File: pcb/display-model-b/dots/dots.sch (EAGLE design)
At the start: 4 parts

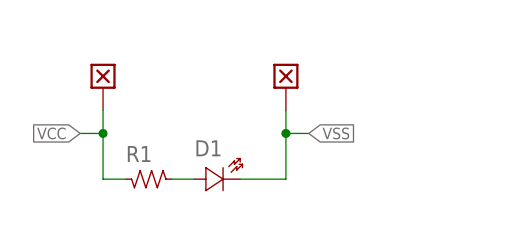
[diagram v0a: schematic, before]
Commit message: Added Model B drawings
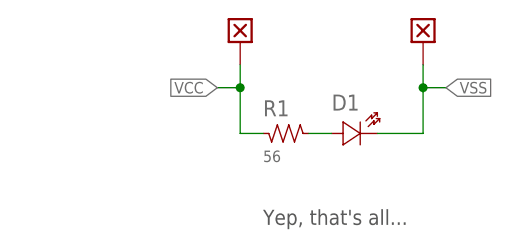
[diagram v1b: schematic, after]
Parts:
- R1: value (none) -> 56
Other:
- note added: "Yep, that's all..."
- moved on the sheet: D1, R1
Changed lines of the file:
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@@
 <schematic xreflabel="%F%N/%S.%C%R" xrefpart="/%S.%C%R">
 <attributes>
+<attribute name="APVD" value=" "/>
+<attribute name="DOC_ID" value="CLK-SCH-06"/>
+<attribute name="DOC_PART_NO" value="CLK-PC-06"/>
+<attribute name="DOC_REV" value="A"/>
+<attribute name="DOC_SUBTITLE" value=" "/>
+<attribute name="DOC_TITLE" value="Dots"/>
+<attribute name="PROJECT_NAME" value="Alarm Clock (Model B)"/>
 </attributes>
 <variantdefs>
@@
 <part name="W1" library="Misc" deviceset="WIRE" device=""/>
 <part name="W2" library="Misc" deviceset="WIRE" device=""/>
-<part name="R1" library="Passive" deviceset="RES" device="-0603"/>
+<part name="R1" library="Passive" deviceset="RES" device="-0603" value="56"/>
 </parts>
 <sheets>
 <sheet>
 <plain>
+<text x="187.96" y="127" size="1.6764" layer="97">Yep, that's all...</text>
 </plain>
 <instances>
 <instance part="FRAME1" gate="G$1" x="0" y="0"/>
-<instance part="D1" gate="G$1" x="182.88" y="132.08"/>
-<instance part="W1" gate="G$1" x="170.18" y="142.24" rot="R90"/>
-<instance part="W2" gate="G$1" x="190.5" y="142.24" rot="R90"/>
-<instance part="R1" gate="A" x="175.26" y="132.08"/>
+<instance part="D1" gate="G$1" x="198.12" y="137.16"/>
+<instance part="W1" gate="G$1" x="185.42" y="147.32" rot="R90"/>
+<instance part="W2" gate="G$1" x="205.74" y="147.32" rot="R90"/>
+<instance part="R1" gate="A" x="190.5" y="137.16"/>
 </instances>
 <busses>
@@
 <segment>
 <pinref part="W1" gate="G$1" pin="P$1"/>
-<wire x1="170.18" y1="139.7" x2="170.18" y2="137.16" width="0.1524" layer="91"/>
+<wire x1="185.42" y1="144.78" x2="185.42" y2="142.24" width="0.1524" layer="91"/>
 <pinref part="R1" gate="A" pin="1"/>
-<wire x1="170.18" y1="137.16" x2="170.18" y2="132.08" width="0.1524" layer="91"/>
-<wire x1="172.72" y1="132.08" x2="170.18" y2="132.08" width="0.1524" layer="91"/>
-<label x="167.64" y="137.16" size="1.27" layer="95" rot="R180" xref="yes"/>
-<wire x1="167.64" y1="137.16" x2="170.18" y2="137.16" width="0.1524" layer="91"/>
-<junction x="170.18" y="137.16"/>
+<wire x1="185.42" y1="142.24" x2="185.42" y2="137.16" width="0.1524" layer="91"/>
+<wire x1="187.96" y1="137.16" x2="185.42" y2="137.16" width="0.1524" layer="91"/>
+<label x="182.88" y="142.24" size="1.27" layer="95" rot="R180" xref="yes"/>
+<wire x1="182.88" y1="142.24" x2="185.42" y2="142.24" width="0.1524" layer="91"/>
+<junction x="185.42" y="142.24"/>
 </segment>
 </net>
@@
 <pinref part="R1" gate="A" pin="2"/>
 <pinref part="D1" gate="G$1" pin="A"/>
-<wire x1="177.8" y1="132.08" x2="180.34" y2="132.08" width="0.1524" layer="91"/>
+<wire x1="193.04" y1="137.16" x2="195.58" y2="137.16" width="0.1524" layer="91"/>
 </segment>
 </net>
@@
 <segment>
 <pinref part="D1" gate="G$1" pin="K"/>
-<wire x1="185.42" y1="132.08" x2="190.5" y2="132.08" width="0.1524" layer="91"/>
+<wire x1="200.66" y1="137.16" x2="205.74" y2="137.16" width="0.1524" layer="91"/>
 <pinref part="W2" gate="G$1" pin="P$1"/>
-<wire x1="190.5" y1="132.08" x2="190.5" y2="137.16" width="0.1524" layer="91"/>
-<label x="193.04" y="137.16" size="1.27" layer="95" xref="yes"/>
-<wire x1="190.5" y1="137.16" x2="190.5" y2="139.7" width="0.1524" layer="91"/>
-<wire x1="190.5" y1="137.16" x2="193.04" y2="137.16" width="0.1524" layer="91"/>
-<junction x="190.5" y="137.16"/>
+<wire x1="205.74" y1="137.16" x2="205.74" y2="142.24" width="0.1524" layer="91"/>
+<label x="208.28" y="142.24" size="1.27" layer="95" xref="yes"/>
+<wire x1="205.74" y1="142.24" x2="205.74" y2="144.78" width="0.1524" layer="91"/>
+<wire x1="205.74" y1="142.24" x2="208.28" y2="142.24" width="0.1524" layer="91"/>
+<junction x="205.74" y="142.24"/>
 </segment>
 </net>

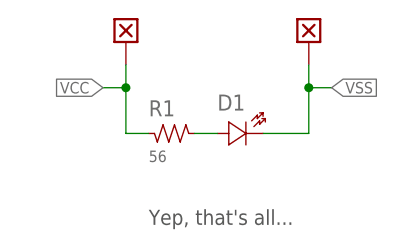
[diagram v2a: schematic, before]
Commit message: Display base pcb (rev C), Touch panel (rev B)
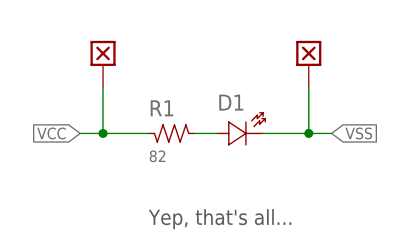
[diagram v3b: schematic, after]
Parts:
- D1: COLOR (none) -> Orange; PART_NO (none) -> APT2012SECK/J4-PRV
- R1: value 56 -> 82
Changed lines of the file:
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@@
 <parts>
 <part name="FRAME1" library="Symbols" deviceset="FRAME_ANSI_B" device=""/>
-<part name="D1" library="Optoelectronic" deviceset="LED" device="-0805" value="{ATTR:COLOR}"/>
+<part name="D1" library="Optoelectronic" deviceset="LED" device="-0805" value="{ATTR:COLOR}">
+<attribute name="COLOR" value="Orange"/>
+<attribute name="PART_NO" value="APT2012SECK/J4-PRV"/>
+</part>
 <part name="W1" library="Misc" deviceset="WIRE" device=""/>
 <part name="W2" library="Misc" deviceset="WIRE" device=""/>
-<part name="R1" library="Passive" deviceset="RES" device="-0603" value="56"/>
+<part name="R1" library="Passive" deviceset="RES" device="-0603" value="82"/>
 </parts>
 <sheets>
@@
 <instances>
 <instance part="FRAME1" gate="G$1" x="0" y="0"/>
-<instance part="D1" gate="G$1" x="198.12" y="137.16"/>
-<instance part="W1" gate="G$1" x="185.42" y="147.32" rot="R90"/>
-<instance part="W2" gate="G$1" x="205.74" y="147.32" rot="R90"/>
+<instance part="D1" gate="G$1" x="198.12" y="137.16">
+<attribute name="PART_NO" x="198.12" y="137.16" size="1.27" layer="96" display="off"/>
+</instance>
+<instance part="W1" gate="G$1" x="182.88" y="144.78" rot="R90"/>
+<instance part="W2" gate="G$1" x="205.74" y="144.78" rot="R90"/>
 <instance part="R1" gate="A" x="190.5" y="137.16"/>
 </instances>
@@
 <segment>
 <pinref part="W1" gate="G$1" pin="P$1"/>
-<wire x1="185.42" y1="144.78" x2="185.42" y2="142.24" width="0.1524" layer="91"/>
+<wire x1="182.88" y1="142.24" x2="182.88" y2="137.16" width="0.1524" layer="91"/>
 <pinref part="R1" gate="A" pin="1"/>
-<wire x1="185.42" y1="142.24" x2="185.42" y2="137.16" width="0.1524" layer="91"/>
-<wire x1="187.96" y1="137.16" x2="185.42" y2="137.16" width="0.1524" layer="91"/>
-<label x="182.88" y="142.24" size="1.27" layer="95" rot="R180" xref="yes"/>
-<wire x1="182.88" y1="142.24" x2="185.42" y2="142.24" width="0.1524" layer="91"/>
-<junction x="185.42" y="142.24"/>
+<wire x1="187.96" y1="137.16" x2="182.88" y2="137.16" width="0.1524" layer="91"/>
+<label x="180.34" y="137.16" size="1.27" layer="95" rot="R180" xref="yes"/>
+<wire x1="180.34" y1="137.16" x2="182.88" y2="137.16" width="0.1524" layer="91"/>
+<junction x="182.88" y="137.16"/>
 </segment>
 </net>
@@
 <wire x1="200.66" y1="137.16" x2="205.74" y2="137.16" width="0.1524" layer="91"/>
 <pinref part="W2" gate="G$1" pin="P$1"/>
+<label x="208.28" y="137.16" size="1.27" layer="95" xref="yes"/>
 <wire x1="205.74" y1="137.16" x2="205.74" y2="142.24" width="0.1524" layer="91"/>
-<label x="208.28" y="142.24" size="1.27" layer="95" xref="yes"/>
-<wire x1="205.74" y1="142.24" x2="205.74" y2="144.78" width="0.1524" layer="91"/>
-<wire x1="205.74" y1="142.24" x2="208.28" y2="142.24" width="0.1524" layer="91"/>
-<junction x="205.74" y="142.24"/>
+<wire x1="205.74" y1="137.16" x2="208.28" y2="137.16" width="0.1524" layer="91"/>
+<junction x="205.74" y="137.16"/>
 </segment>
 </net>

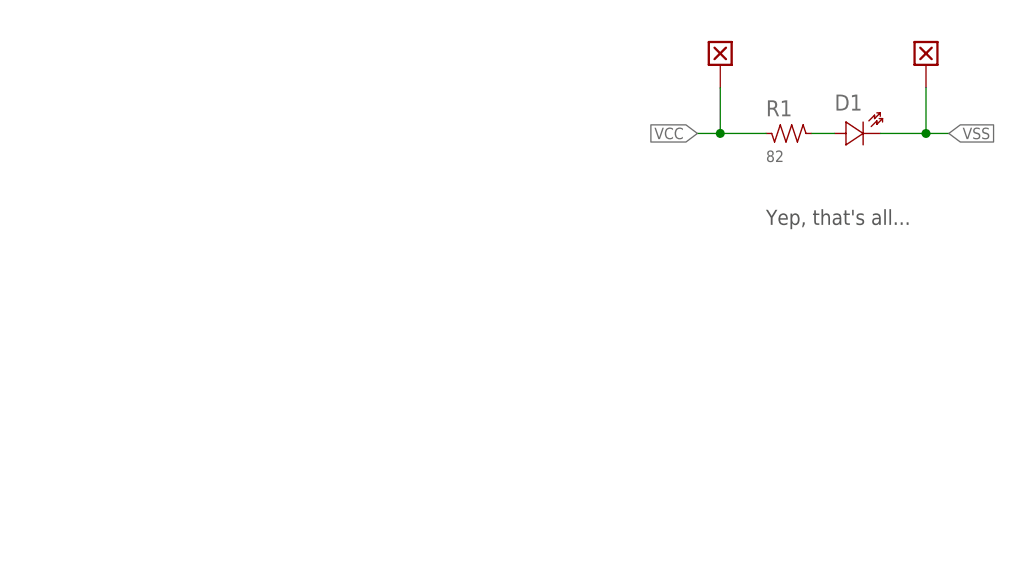
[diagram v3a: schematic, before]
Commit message: Changed page format on schematics to US letter (8.5" x 11")
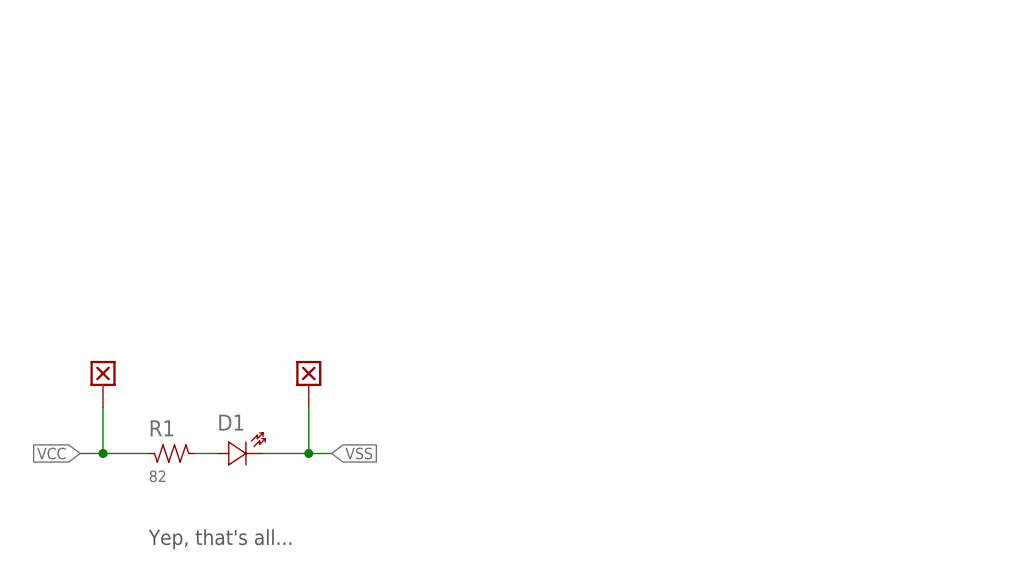
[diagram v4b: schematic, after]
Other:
- moved on the sheet: D1, R1
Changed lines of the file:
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@@
 <schematic xreflabel="%F%N/%S.%C%R" xrefpart="/%S.%C%R">
 <attributes>
-<attribute name="APVD" value=" "/>
+<attribute name="APVD" value="B.F (15-01-03)"/>
 <attribute name="DOC_ID" value="CLK-SCH-06"/>
 <attribute name="DOC_PART_NO" value="CLK-PC-06"/>
@@
 </classes>
 <parts>
-<part name="FRAME1" library="Symbols" deviceset="FRAME_ANSI_B" device=""/>
+<part name="FRAME1" library="Symbols" deviceset="FRAME_LETTER" device=""/>
 <part name="D1" library="Optoelectronic" deviceset="LED" device="-0805" value="{ATTR:COLOR}">
 <attribute name="COLOR" value="Orange"/>
@@
 <sheet>
 <plain>
-<text x="187.96" y="127" size="1.6764" layer="97">Yep, that's all...</text>
+<text x="119.38" y="91.44" size="1.6764" layer="97">Yep, that's all...</text>
 </plain>
 <instances>
 <instance part="FRAME1" gate="G$1" x="0" y="0"/>
-<instance part="D1" gate="G$1" x="198.12" y="137.16">
-<attribute name="PART_NO" x="198.12" y="137.16" size="1.27" layer="96" display="off"/>
+<instance part="D1" gate="G$1" x="129.54" y="101.6">
+<attribute name="PART_NO" x="129.54" y="101.6" size="1.27" layer="96" display="off"/>
 </instance>
-<instance part="W1" gate="G$1" x="182.88" y="144.78" rot="R90"/>
-<instance part="W2" gate="G$1" x="205.74" y="144.78" rot="R90"/>
-<instance part="R1" gate="A" x="190.5" y="137.16"/>
+<instance part="W1" gate="G$1" x="114.3" y="109.22" rot="R90"/>
+<instance part="W2" gate="G$1" x="137.16" y="109.22" rot="R90"/>
+<instance part="R1" gate="A" x="121.92" y="101.6"/>
 </instances>
 <busses>
@@
 <segment>
 <pinref part="W1" gate="G$1" pin="P$1"/>
-<wire x1="182.88" y1="142.24" x2="182.88" y2="137.16" width="0.1524" layer="91"/>
+<wire x1="114.3" y1="106.68" x2="114.3" y2="101.6" width="0.1524" layer="91"/>
 <pinref part="R1" gate="A" pin="1"/>
-<wire x1="187.96" y1="137.16" x2="182.88" y2="137.16" width="0.1524" layer="91"/>
-<label x="180.34" y="137.16" size="1.27" layer="95" rot="R180" xref="yes"/>
-<wire x1="180.34" y1="137.16" x2="182.88" y2="137.16" width="0.1524" layer="91"/>
-<junction x="182.88" y="137.16"/>
+<wire x1="119.38" y1="101.6" x2="114.3" y2="101.6" width="0.1524" layer="91"/>
+<label x="111.76" y="101.6" size="1.27" layer="95" rot="R180" xref="yes"/>
+<wire x1="111.76" y1="101.6" x2="114.3" y2="101.6" width="0.1524" layer="91"/>
+<junction x="114.3" y="101.6"/>
 </segment>
 </net>
@@
 <pinref part="R1" gate="A" pin="2"/>
 <pinref part="D1" gate="G$1" pin="A"/>
-<wire x1="193.04" y1="137.16" x2="195.58" y2="137.16" width="0.1524" layer="91"/>
+<wire x1="124.46" y1="101.6" x2="127" y2="101.6" width="0.1524" layer="91"/>
 </segment>
 </net>
@@
 <segment>
 <pinref part="D1" gate="G$1" pin="K"/>
-<wire x1="200.66" y1="137.16" x2="205.74" y2="137.16" width="0.1524" layer="91"/>
+<wire x1="132.08" y1="101.6" x2="137.16" y2="101.6" width="0.1524" layer="91"/>
 <pinref part="W2" gate="G$1" pin="P$1"/>
-<label x="208.28" y="137.16" size="1.27" layer="95" xref="yes"/>
-<wire x1="205.74" y1="137.16" x2="205.74" y2="142.24" width="0.1524" layer="91"/>
-<wire x1="205.74" y1="137.16" x2="208.28" y2="137.16" width="0.1524" layer="91"/>
-<junction x="205.74" y="137.16"/>
+<label x="139.7" y="101.6" size="1.27" layer="95" xref="yes"/>
+<wire x1="137.16" y1="101.6" x2="137.16" y2="106.68" width="0.1524" layer="91"/>
+<wire x1="137.16" y1="101.6" x2="139.7" y2="101.6" width="0.1524" layer="91"/>
+<junction x="137.16" y="101.6"/>
 </segment>
 </net>
